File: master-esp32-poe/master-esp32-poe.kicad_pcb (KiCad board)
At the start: 2 copper layers, 61 x 72.4 mm, 9 parts, among them J1 24V Field, J2 24V System, J3 Conn_01x06_Female, J4 Conn_01x06_Female, J5 Screw_Terminal_01x03, SW1 SW_DIP_x02, U1 LM2596-Board, U2 ESP32-POE

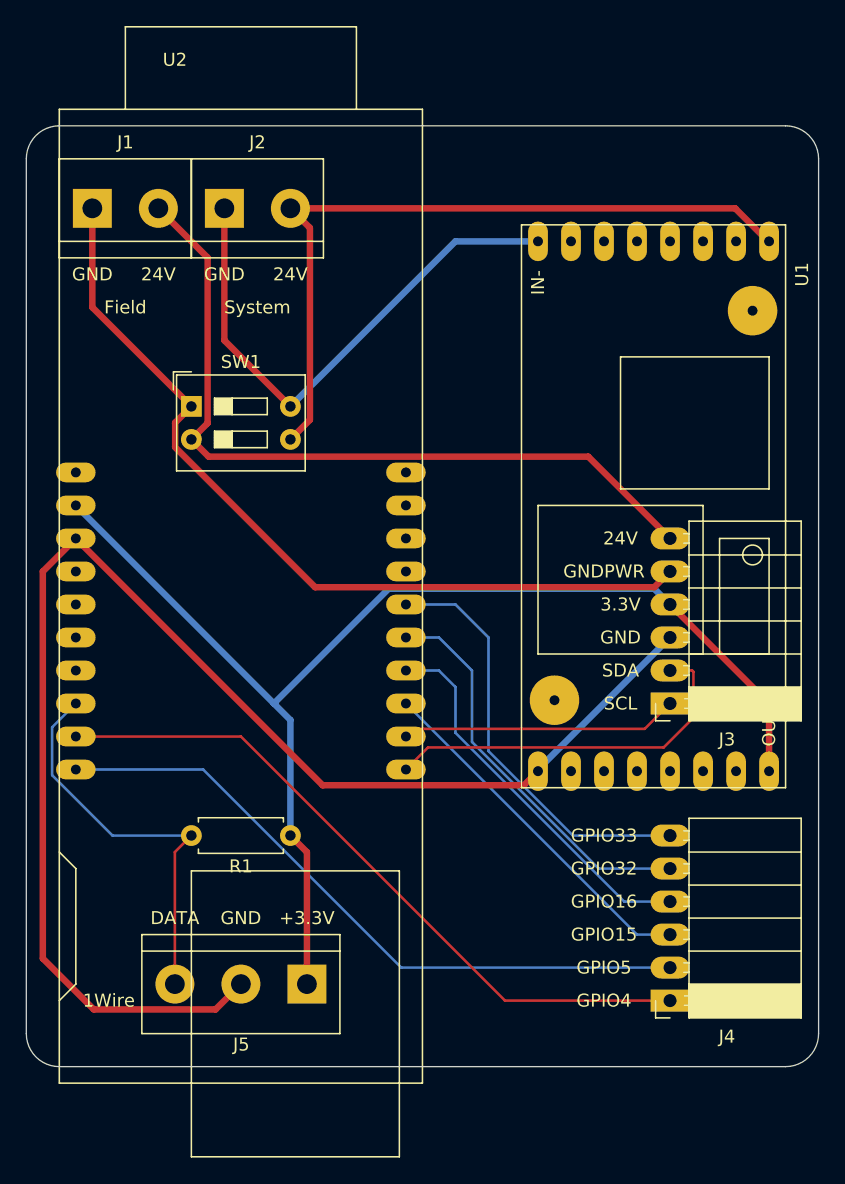
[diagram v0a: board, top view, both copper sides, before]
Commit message: fix terminal blocks
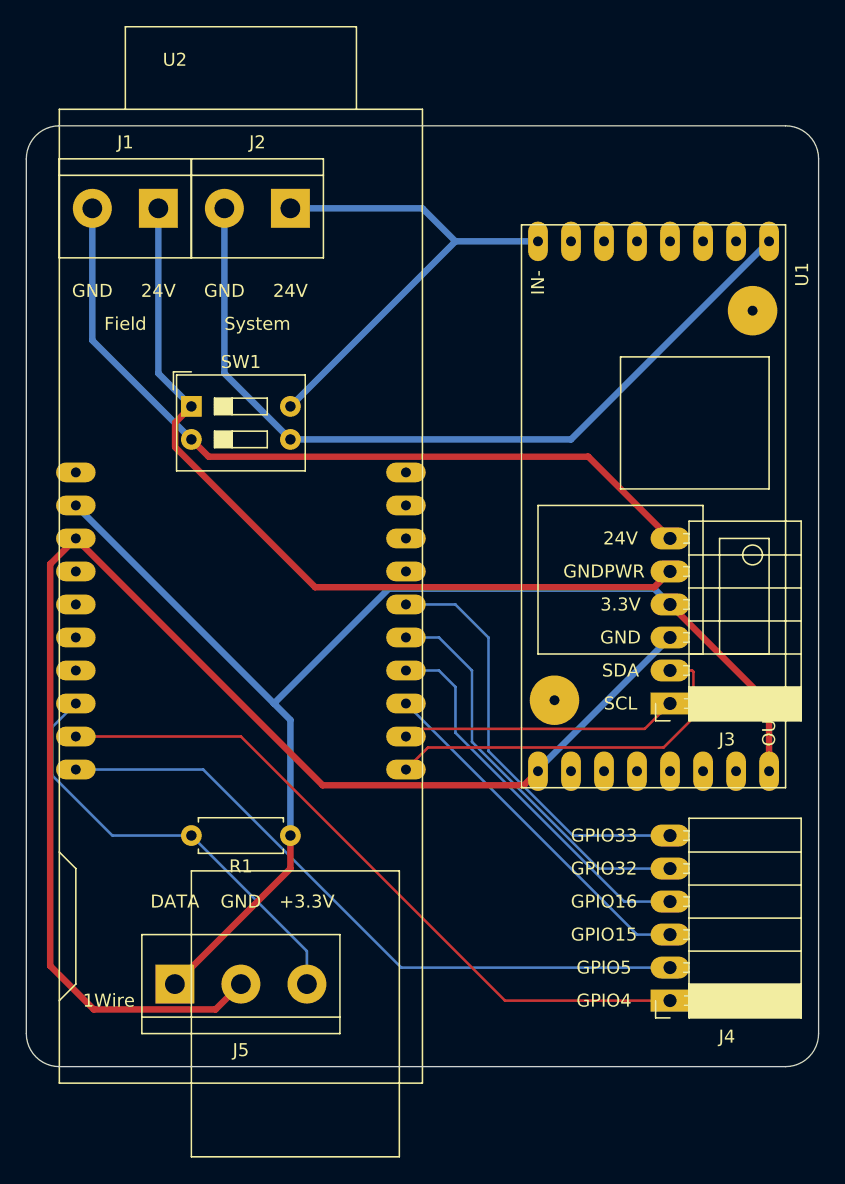
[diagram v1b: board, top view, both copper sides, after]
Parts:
- moved J5 10.2 mm to (74.9, 120.7), turned to 0 degrees
- moved J1 5.08 mm to (73.7, 61.0), turned to 180 degrees
- moved J2 5.08 mm to (83.8, 61.0), turned to 180 degrees
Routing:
- net Net-(J2-Pad2): track 56.9 -> 63.1 mm
- net Net-(J2-Pad1): track 41.7 -> 38.1 mm
- net 1WIRE: track 30.9 -> 34.0 mm
- net +3V3: track 94.8 -> 98.0 mm
- net GNDPWR: track 65.1 -> 63.0 mm
- net +24V: track 59.9 -> 60.9 mm

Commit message: upgrade master-esp32-poe format
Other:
- net class Default removed
- net class Power removed
